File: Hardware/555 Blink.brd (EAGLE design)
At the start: 100 x 80 mm, 10 parts, among them IC1 LM555N

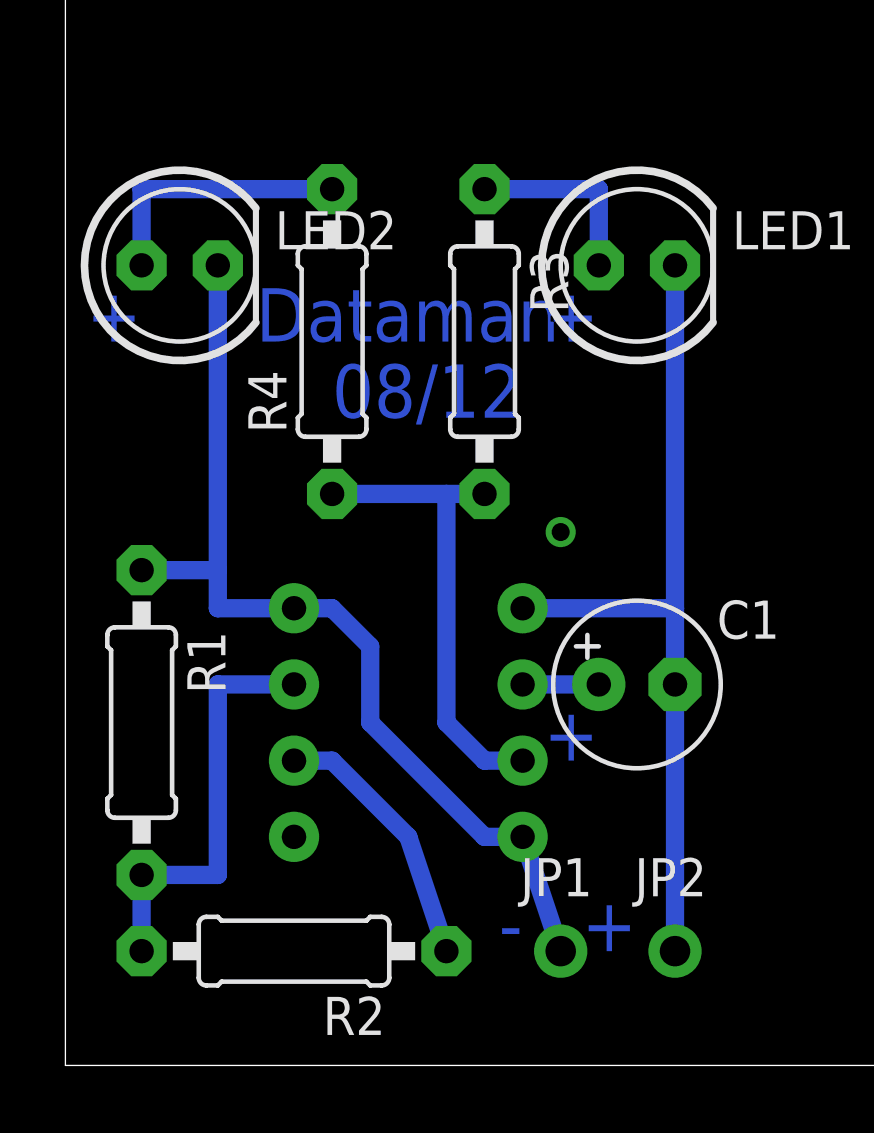
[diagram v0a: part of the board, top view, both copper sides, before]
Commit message: Fixup
Flip Positive LED
Connect 2 to 6
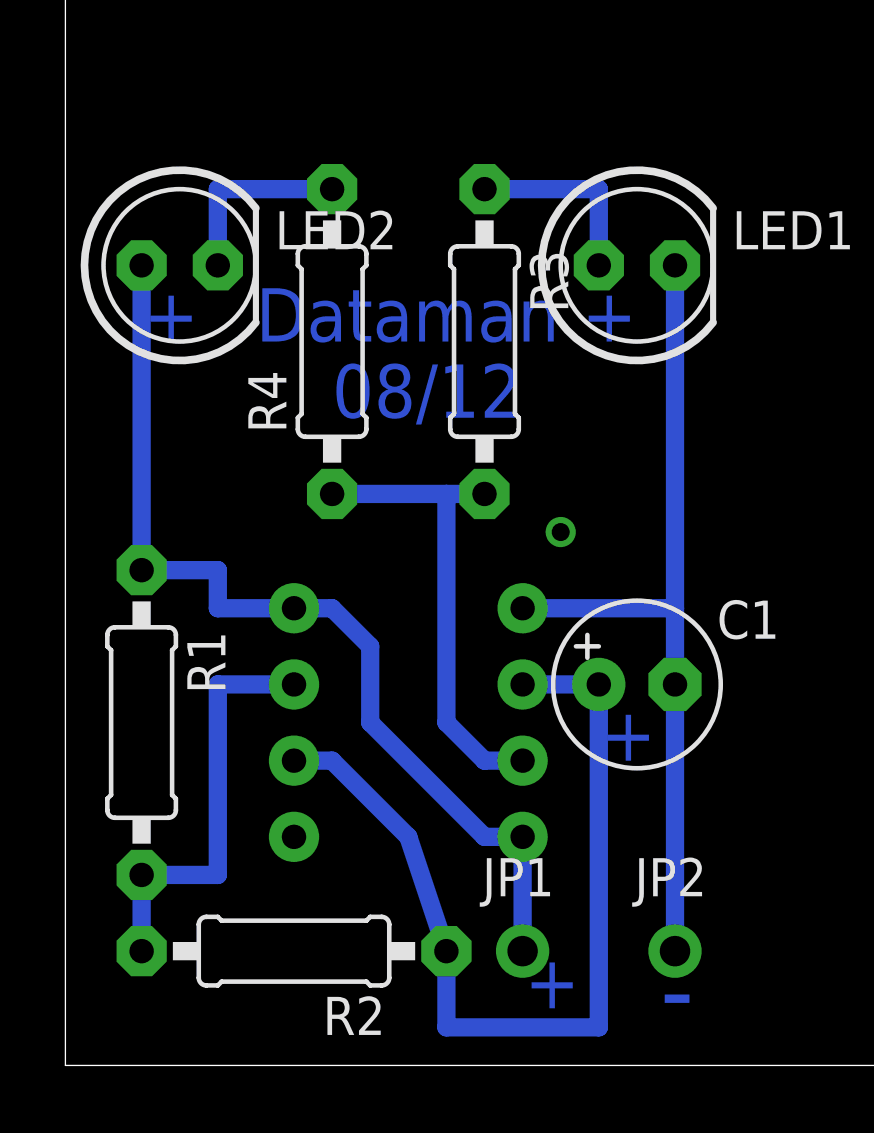
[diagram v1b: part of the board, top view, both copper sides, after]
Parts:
- moved JP1 1.27 mm to (15.2, 3.81)
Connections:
- removed net N$5: C1.+, IC1.2
- removed net N$7: LED2.A, R4.2
- new net N$4: LED2.K, R4.2
- net +9V: now also LED2.A; no longer LED2.K
- net N$2: now also C1.+, IC1.2
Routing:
- net N$2: track 8.88 -> 30.5 mm
- net N$7: track 8.89 -> 0.00 mm
- net N$4: track 0.00 -> 6.35 mm
- net N$5: track 2.54 -> 0.00 mm
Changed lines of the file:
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@@
 <wire x1="100" y1="80" x2="0" y2="80" width="0" layer="20"/>
 <wire x1="0" y1="80" x2="0" y2="0" width="0" layer="20"/>
-<text x="2.54" y="24.13" size="1.778" layer="16" rot="MR0">+</text>
-<text x="17.78" y="24.13" size="1.778" layer="16" rot="MR0">+</text>
-<text x="17.78" y="10.16" size="1.778" layer="16" rot="MR0">+</text>
-<text x="19.05" y="3.81" size="1.778" layer="16" rot="MR0">+</text>
+<text x="4.445" y="24.13" size="1.778" layer="16" rot="MR0">+</text>
+<text x="19.05" y="24.13" size="1.778" layer="16" rot="MR0">+</text>
+<text x="19.685" y="10.16" size="1.778" layer="16" rot="MR0">+</text>
+<text x="17.145" y="1.905" size="1.778" layer="16" rot="MR0">+</text>
 <text x="6.35" y="24.13" size="1.778" layer="16">Dataman</text>
 <text x="8.89" y="21.59" size="1.778" layer="16">08/12</text>
-<text x="15.24" y="3.81" size="1.778" layer="16" rot="MR0">-</text>
+<text x="20.955" y="1.27" size="2.54" layer="16" rot="MR0">-</text>
 </plain>
 <attributes>
@@
 <element name="LED1" library="adafruit" package="LED5MM" value="" x="19.05" y="26.67"/>
 <element name="LED2" library="adafruit" package="LED5MM" value="" x="3.81" y="26.67"/>
-<element name="JP1" library="adafruit" package="1X01-CLEANBIG" value="" x="16.51" y="3.81"/>
+<element name="JP1" library="adafruit" package="1X01-CLEANBIG" value="" x="15.24" y="3.81"/>
 <element name="JP2" library="adafruit" package="1X01-CLEANBIG" value="" x="20.32" y="3.81"/>
 </elements>
 <signals>
-<signal name="N$2">
-<contactref element="IC1" pad="6"/>
-<contactref element="R2" pad="1"/>
-<wire x1="12.7" y1="3.81" x2="11.43" y2="7.62" width="0.6096" layer="16"/>
-<wire x1="11.43" y1="7.62" x2="8.89" y2="10.16" width="0.6096" layer="16"/>
-<wire x1="8.89" y1="10.16" x2="7.62" y2="10.16" width="0.6096" layer="16"/>
-</signal>
 <signal name="N$3">
 <contactref element="IC1" pad="7"/>
@@
 <wire x1="5.08" y1="6.35" x2="5.08" y2="12.7" width="0.6096" layer="16"/>
 <wire x1="5.08" y1="12.7" x2="7.62" y2="12.7" width="0.6096" layer="16"/>
-</signal>
-<signal name="N$5">
-<contactref element="IC1" pad="2"/>
-<contactref element="C1" pad="+"/>
-<wire x1="17.78" y1="12.7" x2="15.24" y2="12.7" width="0.6096" layer="16"/>
 </signal>
 <signal name="GND">
@@
 <contactref element="R1" pad="1"/>
 <contactref element="IC1" pad="4"/>
-<contactref element="LED2" pad="K"/>
 <contactref element="JP1" pad="1"/>
-<wire x1="5.08" y1="26.67" x2="5.08" y2="16.51" width="0.6096" layer="16"/>
 <wire x1="2.54" y1="16.51" x2="5.08" y2="16.51" width="0.6096" layer="16"/>
 <wire x1="5.08" y1="16.51" x2="5.08" y2="15.24" width="0.6096" layer="16"/>
@@
 <wire x1="10.16" y1="11.43" x2="13.97" y2="7.62" width="0.6096" layer="16"/>
 <wire x1="13.97" y1="7.62" x2="15.24" y2="7.62" width="0.6096" layer="16"/>
-<wire x1="16.51" y1="3.81" x2="15.24" y2="7.62" width="0.6096" layer="16"/>
+<wire x1="15.24" y1="3.81" x2="15.24" y2="7.62" width="0.6096" layer="16"/>
+<contactref element="LED2" pad="A"/>
+<wire x1="2.54" y1="26.67" x2="2.54" y2="16.51" width="0.6096" layer="16"/>
 </signal>
 <signal name="N$1">
@@
 <wire x1="17.78" y1="29.21" x2="13.97" y2="29.21" width="0.6096" layer="16"/>
 </signal>
-<signal name="N$7">
-<contactref element="R4" pad="2"/>
-<contactref element="LED2" pad="A"/>
-<wire x1="2.54" y1="26.67" x2="2.54" y2="29.21" width="0.6096" layer="16"/>
-<wire x1="2.54" y1="29.21" x2="8.89" y2="29.21" width="0.6096" layer="16"/>
-</signal>
 <signal name="N$4">
 <via x="16.51" y="17.78" extent="1-16" drill="0.6"/>
+<contactref element="R4" pad="2"/>
+<contactref element="LED2" pad="K"/>
+<wire x1="16.51" y1="17.78" x2="8.89" y2="29.21" width="0" layer="19" extent="1-1"/>
+<wire x1="5.08" y1="26.67" x2="5.08" y2="29.21" width="0.6096" layer="16"/>
+<wire x1="5.08" y1="29.21" x2="8.89" y2="29.21" width="0.6096" layer="16"/>
+</signal>
+<signal name="N$2">
+<contactref element="IC1" pad="2"/>
+<contactref element="C1" pad="+"/>
+<contactref element="IC1" pad="6"/>
+<contactref element="R2" pad="1"/>
+<wire x1="17.78" y1="12.7" x2="15.24" y2="12.7" width="0.6096" layer="16"/>
+<wire x1="12.7" y1="3.81" x2="11.43" y2="7.62" width="0.6096" layer="16"/>
+<wire x1="11.43" y1="7.62" x2="8.89" y2="10.16" width="0.6096" layer="16"/>
+<wire x1="8.89" y1="10.16" x2="7.62" y2="10.16" width="0.6096" layer="16"/>
+<wire x1="17.78" y1="12.7" x2="17.78" y2="1.27" width="0.6096" layer="16"/>
+<wire x1="17.78" y1="1.27" x2="12.7" y2="1.27" width="0.6096" layer="16"/>
+<wire x1="12.7" y1="1.27" x2="12.7" y2="3.81" width="0.6096" layer="16"/>
 </signal>
 </signals>
